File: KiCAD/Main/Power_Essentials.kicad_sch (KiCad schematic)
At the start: 24 parts, among them J1 Micro_SD_Card_Det2, J2 Screw_Terminal_01x09, J3 Screw_Terminal_01x09, J4 USB_C_Receptacle_USB2.0_16P, Q1 AO3400A, Q2 AO3400A, Q3 AO3400A, U1 LM2596S-3.3, U2 TPS2121RUXR

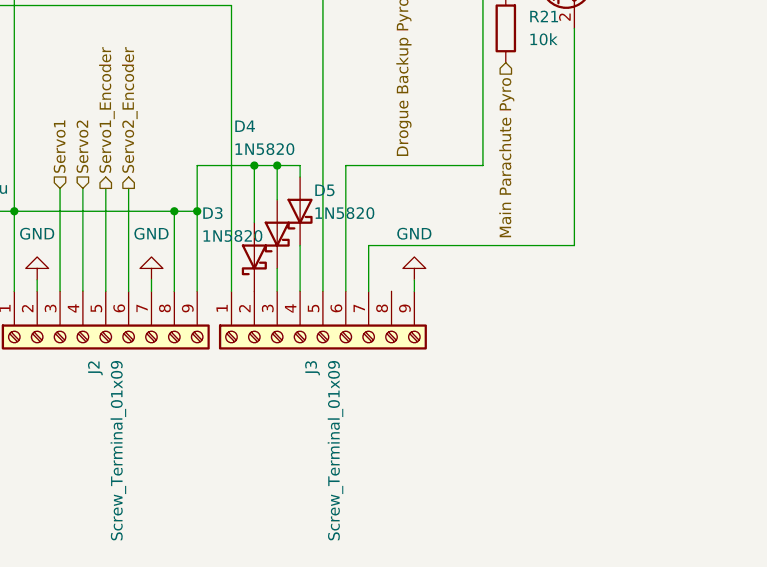
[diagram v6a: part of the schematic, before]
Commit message: Update wiring diagram with TM input
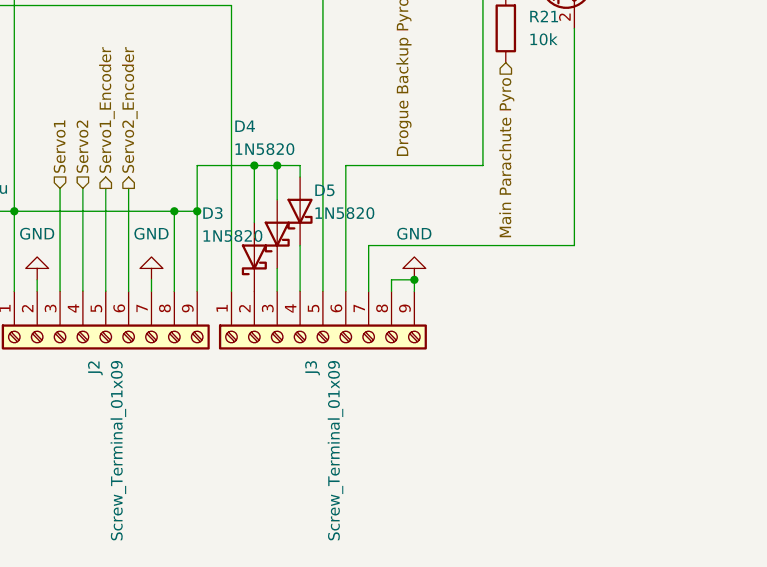
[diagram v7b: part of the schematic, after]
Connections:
- net GND: now also J3.8 (Pin_8)
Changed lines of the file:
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@@
+	)
+	(junction
+		(at 248.92 127)
+		(diameter 0)
+		(color 0 0 0 0)
 	)
 	(junction
@@
 	(wire
 		(pts
+			(xy 246.38 127) (xy 246.38 128.27)
+		)
+		(stroke
+			(width 0)
+			(type default)
+		)
+	)
+	(wire
+		(pts
 			(xy 208.28 80.01) (xy 204.47 80.01)
 		)
@@
 		(pts
 			(xy 181.61 41.91) (xy 181.61 69.85)
+		)
+		(stroke
+			(width 0)
+			(type default)
+		)
+	)
+	(wire
+		(pts
+			(xy 248.92 127) (xy 246.38 127)
 		)
 		(stroke
@@
 	)
 	(symbol
+		(lib_id "power:GND")
+		(at 248.92 127 180)
+		(unit 1)
+		(exclude_from_sim no)
+		(in_bom yes)
+		(on_board yes)
+		(dnp no)
+		(property "Reference" "#PWR066"
+			(at 248.92 120.65 0)
+			(effects
+				(font
+					(size 1.27 1.27)
+				)
+				(hide yes)
+			)
+		)
+		(property "Value" "GND"
+			(at 248.92 121.92 0)
+			(effects
+				(font
+					(size 1.27 1.27)
+				)
+			)
+		)
+		(property "Footprint" ""
+			(at 248.92 127 0)
+			(effects
+				(font
+					(size 1.27 1.27)
+				)
+				(hide yes)
+			)
+		)
+		(property "Datasheet" ""
+			(at 248.92 127 0)
+			(effects
+				(font
+					(size 1.27 1.27)
+				)
+				(hide yes)
+			)
+		)
+		(property "Description" "Power symbol creates a global label with name \"GND\" , ground"
+			(at 248.92 127 0)
+			(effects
+				(font
+					(size 1.27 1.27)
+				)
+				(hide yes)
+			)
+		)
+		(pin "1"
+		)
+		(instances
+			(project "Main"
+				(path "/bbb10697-a5dd-43b8-9c6f-4c5919cf3463/14279dde-67ce-4c97-8b3d-bab2d340dd8b"
+					(reference "#PWR066")
+					(unit 1)
+				)
+			)
+		)
+	)
+	(symbol
 		(lib_id "power:+3V3")
 		(at 87.63 50.8 180)
@@
 					(unit 1)
 				)
-			)
-		)
-	)
-	(symbol
-		(lib_id "power:GND")
-		(at 248.92 127 180)
-		(unit 1)
-		(exclude_from_sim no)
-		(in_bom yes)
-		(on_board yes)
-		(dnp no)
-		(property "Reference" "#PWR023"
-			(at 248.92 120.65 0)
-			(effects
-				(font
-					(size 1.27 1.27)
-				)
-				(hide yes)
-			)
-		)
-		(property "Value" "GND"
-			(at 248.92 121.92 0)
-			(effects
-				(font
-					(size 1.27 1.27)
-				)
-			)
-		)
-		(property "Footprint" ""
-			(at 248.92 127 0)
-			(effects
-				(font
-					(size 1.27 1.27)
-				)
-				(hide yes)
-			)
-		)
-		(property "Datasheet" ""
-			(at 248.92 127 0)
-			(effects
-				(font
-					(size 1.27 1.27)
-				)
-				(hide yes)
-			)
-		)
-		(property "Description" "Power symbol creates a global label with name \"GND\" , ground"
-			(at 248.92 127 0)
-			(effects
-				(font
-					(size 1.27 1.27)
-				)
-				(hide yes)
-			)
-		)
-		(pin "1"
-		)
-		(instances
-			(project ""
-				(path "/bbb10697-a5dd-43b8-9c6f-4c5919cf3463/14279dde-67ce-4c97-8b3d-bab2d340dd8b"
-					(reference "#PWR023")
-					(unit 1)
-				)

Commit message: Submit design for review
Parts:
- added D7: MBRS340, Diode_SMD:D_SMC, symbol Diode:MBRS340
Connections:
- net at J4.A4 (VBUS), J4.A9 (VBUS), J4.B4 (VBUS)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: now also D7.2 (A); no longer U2.7 (IN1), U2.7_1 (IN1)
- new net +5V: D7.1 (K), U2.7 (IN1), U2.7_1 (IN1)
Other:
- moved on the sheet: J1, R3
